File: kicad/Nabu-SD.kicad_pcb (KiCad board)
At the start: 2 copper layers, 127 x 53.2 mm, 63 parts, among them J1 Nabu Expansion Slot, J10 USB_B_Micro, J2 ICSP, J3 SD Card, J4 Serial, J5 I2C, J6 OUT1, J7 SD Card, J8A1 XKTF-005, J8B1 XKTF-0803-0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

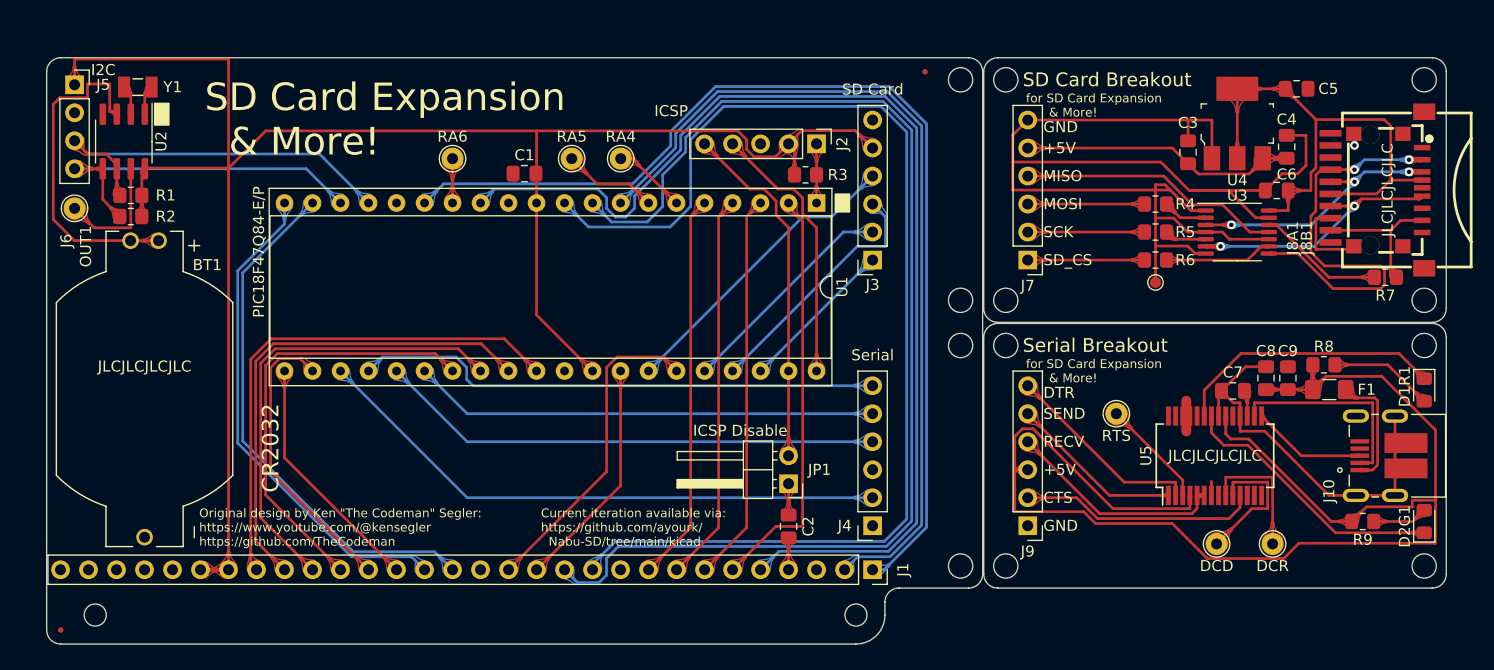
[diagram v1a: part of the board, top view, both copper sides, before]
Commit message: Shuffled around PIC pins around for I2C and Serial CTS signals to be more inline with the datasheet for this specific PIC.
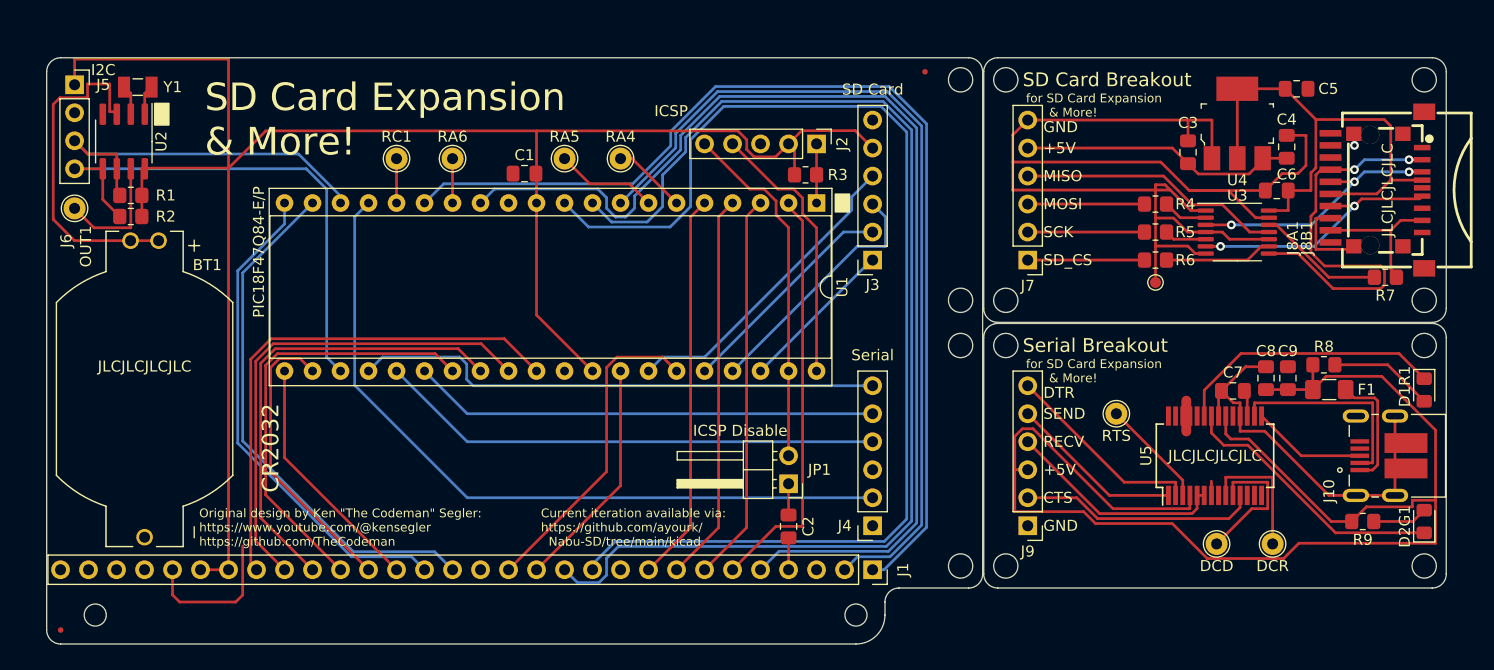
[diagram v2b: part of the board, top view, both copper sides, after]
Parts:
- added RC1: TestPoint_THTPad_D2.0mm_Drill1.0mm, TestPoint:TestPoint_THTPad_D2.0mm_Drill1.0mm, F.Cu at (74.4, 43.0)
- moved RA5 0.65 mm to (89.6, 43.0)
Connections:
- J4 pad 2: /RC4 -> /RC2
- J9 pad 2: /RC4 -> /RC2
- U1 pad 17: /SCL -> /RC2
- U1 pad 18: /SDA -> /SCL
- U1 pad 23: /RC4 -> /SDA
- U5 pad 11: /RC4 -> /RC2
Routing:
- net /RC2: track 0.00 -> 89.8 mm
- net /RC4: track 74.6 -> 0.00 mm
- net /SDA: track 32.9 -> 48.2 mm
- net GND: track 162.3 -> 175.9 mm
- net /RC1: track 0.00 -> 4.03 mm
- net /SCL: track 36.6 -> 35.0 mm
- net /MISO: track 51.6 -> 52.3 mm
- net /RA5: track 8.64 -> 9.29 mm
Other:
- board text added: "RC2 --> CTS Serial?"
- board text added: "RC3 --> SCL?"
- board text added: "RC4 --> SDA? vs CTS Serial"

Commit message: Update +5V and +3V3 voltage trace widths per @K3130440 and greghol.
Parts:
- added C10: 10uF, Capacitor_SMD:C_0805_2012Metric_Pad1.18x1.45mm_HandSolder, F.Cu at (58.1, 48.4)
- moved R7 0.07 mm to (164.0, 53.8)
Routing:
- net GND: track 175.9 -> 237.7 mm
- net /D0: track 48.1 -> 38.5 mm
- net /D1: track 45.2 -> 38.5 mm
- net +3V3: track 47.6 -> 48.6 mm

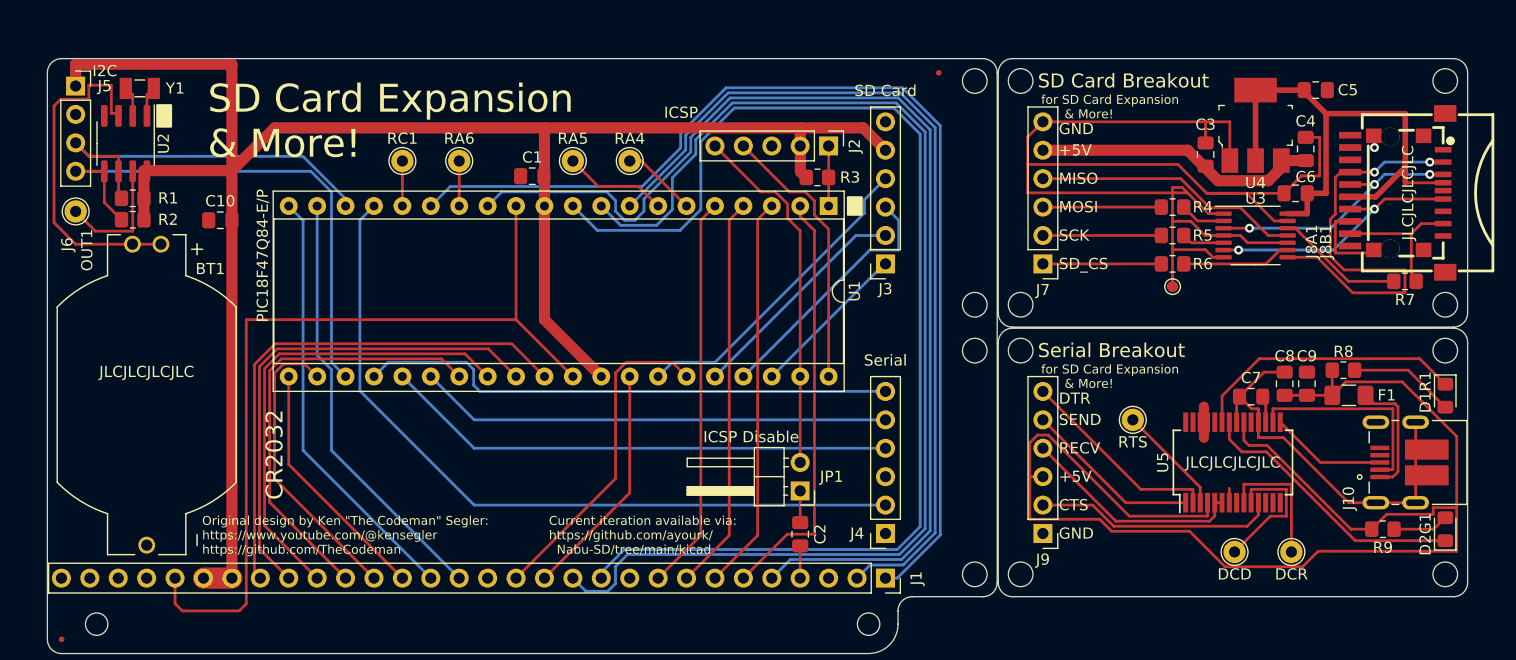
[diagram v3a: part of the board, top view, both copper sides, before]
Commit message: Added Teardrops.
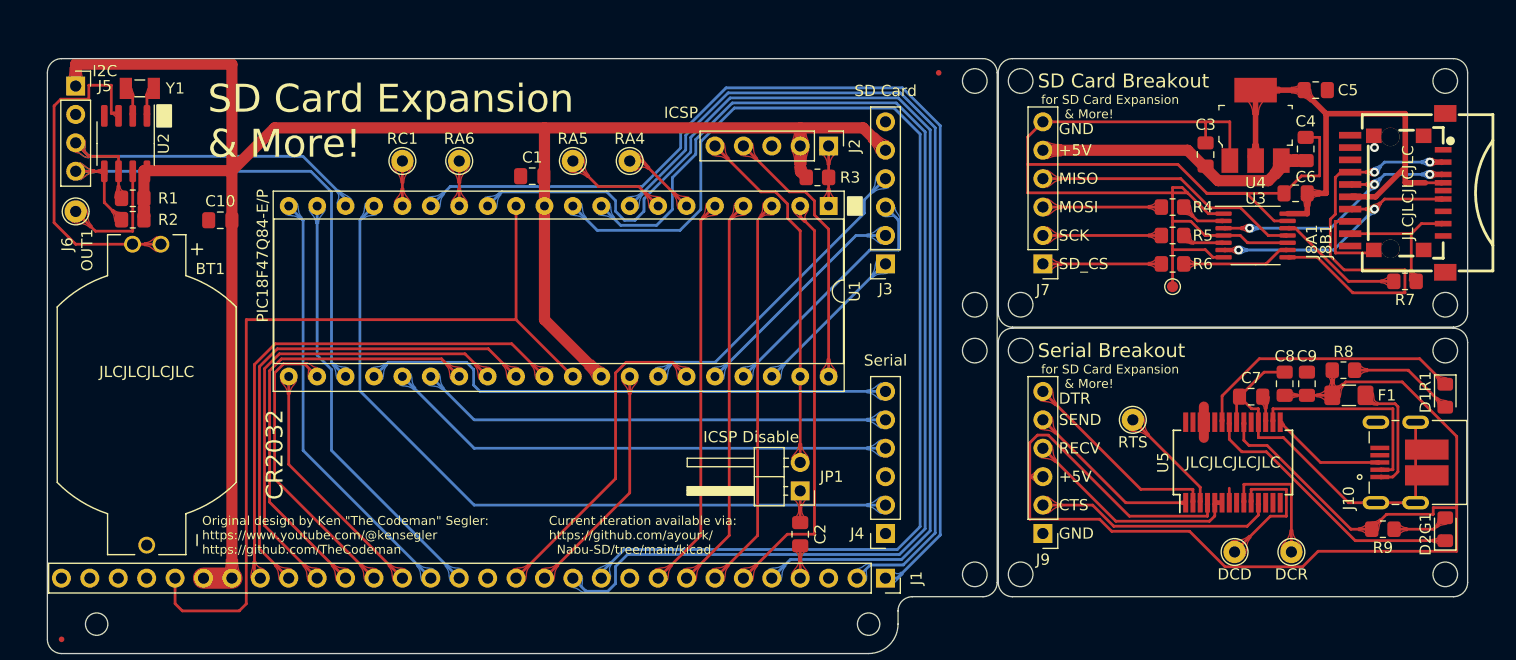
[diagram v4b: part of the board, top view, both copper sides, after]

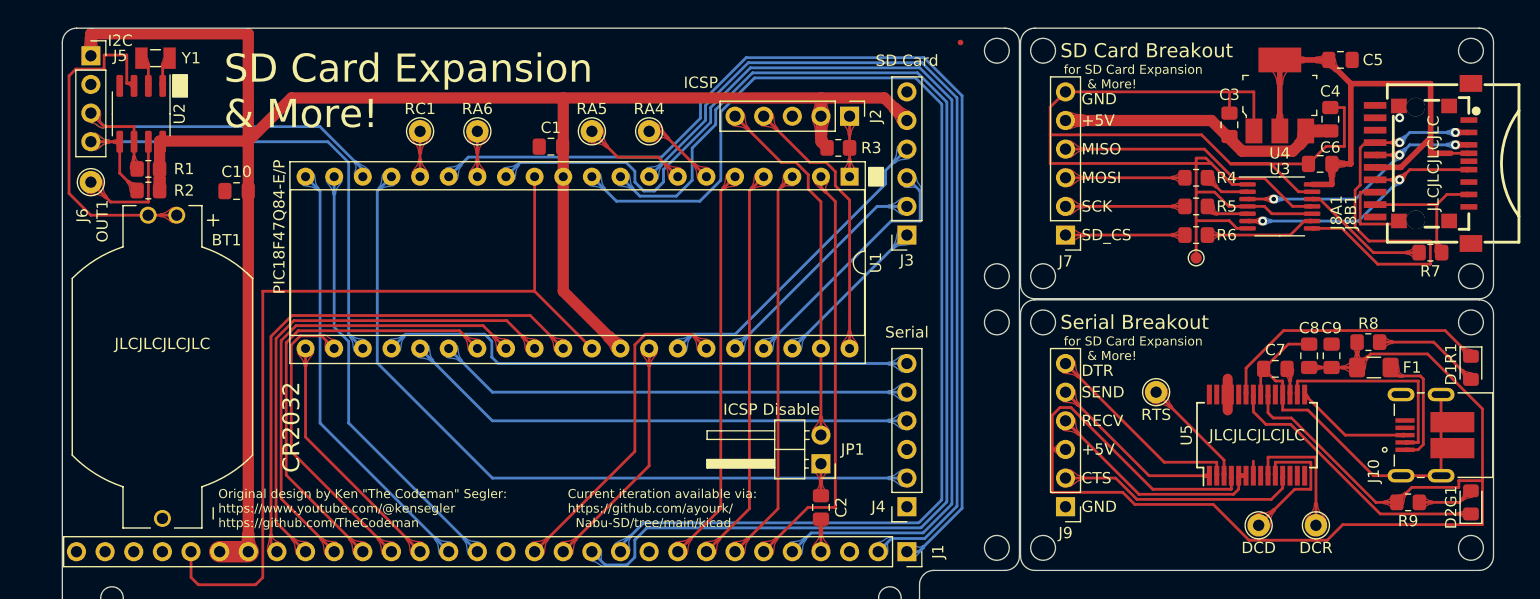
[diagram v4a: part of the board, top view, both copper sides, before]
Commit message: Added Vias and test points for Serial Breakout board.
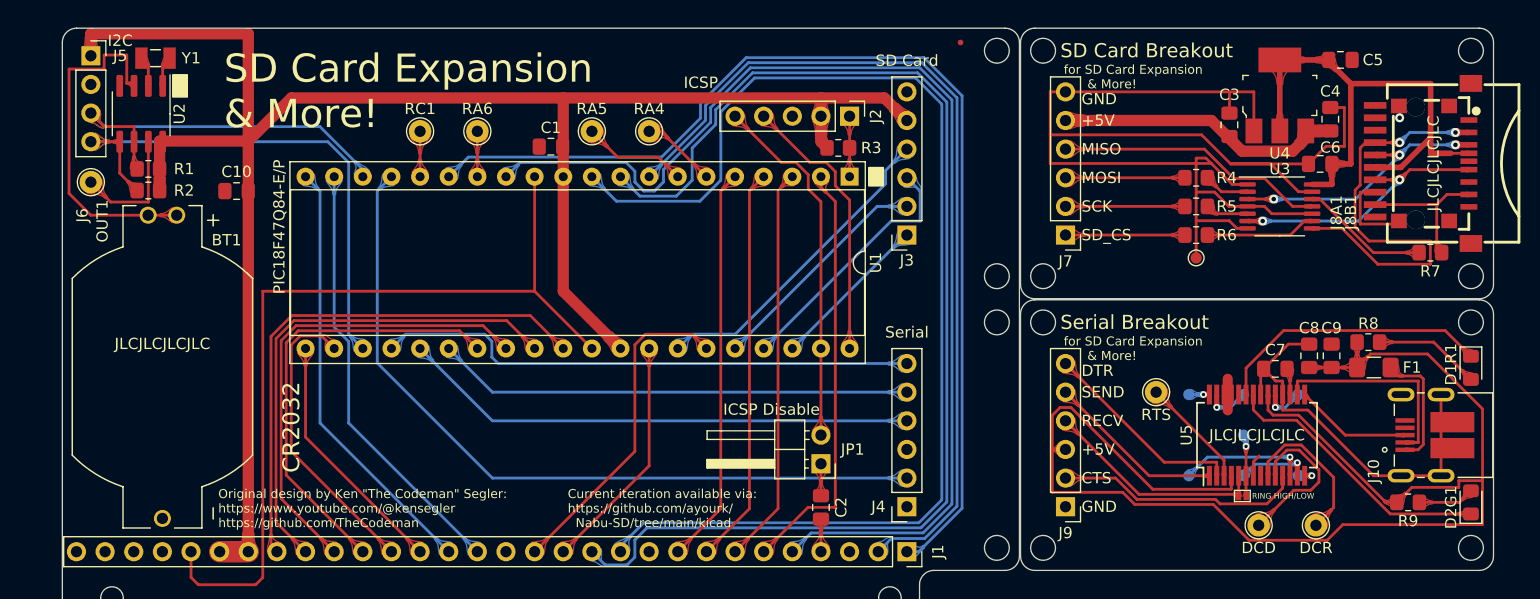
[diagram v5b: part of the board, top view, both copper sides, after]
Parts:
- added OSCI: TestPoint_Pad_D1.0mm, TestPoint:TestPoint_Pad_D1.0mm, B.Cu at (147.4, 66.4)
- added OSCO: TestPoint_Pad_D1.0mm, TestPoint:TestPoint_Pad_D1.0mm, B.Cu at (142.6, 66.4)
- added PWREN: TestPoint_Pad_D1.0mm, TestPoint:TestPoint_Pad_D1.0mm, B.Cu at (147.4, 73.6)
- added RESET: TestPoint_Pad_D1.0mm, TestPoint:TestPoint_Pad_D1.0mm, B.Cu at (152.3, 66.4)
- added RING HIGH/LOW: SolderJumper-2_P0.65mm_Bridged2Bar_Pad0.5x0.75mm, A_Personal_Library:SolderJumper-2_P0.65mm_Bridged1Bar_Pad0.5x0.75mm, F.Cu at (147.3, 75.4)
- added RING INDICATOR: TestPoint_Pad_D1.0mm, TestPoint:TestPoint_Pad_D1.0mm, B.Cu at (147.4, 70.0)
- added SLEEP: TestPoint_Pad_D1.0mm, TestPoint:TestPoint_Pad_D1.0mm, B.Cu at (142.6, 73.6)
- added TXDEN: TestPoint_Pad_D1.0mm, TestPoint:TestPoint_Pad_D1.0mm, B.Cu at (152.3, 73.6)
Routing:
- net /Serial_Breakout/SLEEP: track 0.00 -> 11.3 mm, vias 0 -> 1
- net /Serial_Breakout/PWREN: track 0.00 -> 6.40 mm, vias 0 -> 1
- net /RX1: track 65.9 -> 71.2 mm, vias 0 -> 1
- net /Serial_Breakout/OSCI: track 0.00 -> 3.99 mm, vias 0 -> 1
- net /Serial_Breakout/~{RESET}: track 0.00 -> 3.64 mm, vias 0 -> 1
- net /Serial_Breakout/TXDEN: track 0.00 -> 1.83 mm, vias 0 -> 1
- net /Serial_Breakout/DCR: track 11.9 -> 13.8 mm
- net /Serial_Breakout/OSCO: track 0.00 -> 1.82 mm, vias 0 -> 1
- net /Serial_Breakout/DCD: track 12.7 -> 14.3 mm
- net GND: track 237.7 -> 239.2 mm
